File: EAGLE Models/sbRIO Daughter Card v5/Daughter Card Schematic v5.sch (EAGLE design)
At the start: 67 parts, among them IC1 BTS716G, IC2 BTS716G, IC3 BTS716G, Q7 MMBT4403-7-F, Q8 MMBT4403-7-F, U2 ADXL345, U3 L3G4200D

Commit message: made more changes to daughter card
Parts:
- removed F10, F9: (no value), resistor:R-EU_R0402
- added F11, F12: (no value), resistor:R-EU_R0402
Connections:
- removed net N$22: F9.1, TUB_CONN-12.KL
- removed net N$23: F10.1, TUB_CONN-5.KL
- new net N$7: F11.1, TUB_CONN-3.KL
- new net N$8: F12.1, TUB_CONN-1.KL
- net 12V: now also F11.2
- net 5V: now also F12.2; no longer F10.2, F9.2
- net AI3: now also TUB_CONN-11.KL; no longer TUB_CONN-10.KL
- net AI4: now also TUB_CONN-12.KL; no longer TUB_CONN-9.KL
- net AMS_OUT: now also TUB_CONN-6.KL; no longer TUB_CONN-3.KL
- net BSPD_OUT: now also TUB_CONN-4.KL; no longer TUB_CONN-1.KL
- net BUZZER_OUT: now also TUB_CONN-7.KL; no longer TUB_CONN-4.KL
- net CAN_H: now also TUB_CONN-9.KL; no longer TUB_CONN-7.KL
- net CAN_L: now also TUB_CONN-8.KL; no longer TUB_CONN-6.KL
- net DI02: now also TUB_CONN-2.KL; no longer TUB_CONN-8.KL
- net GND: now also TUB_CONN-10.KL; no longer TUB_CONN-11.KL
- net IMD_OUT: now also TUB_CONN-5.KL; no longer TUB_CONN-2.KL
- net STEERING_POS: now also TUB_CONN-16.KL; no longer TUB_CONN-14.KL
- net THROTTLE_1: now also TUB_CONN-15.KL; no longer TUB_CONN-16.KL
- net THROTTLE_2: now also TUB_CONN-14.KL; no longer TUB_CONN-15.KL
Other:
- moved on the sheet: R36, TUB_CONN-1, TUB_CONN-10, TUB_CONN-11, TUB_CONN-12, TUB_CONN-13, TUB_CONN-14, TUB_CONN-15, TUB_CONN-16, TUB_CONN-2, TUB_CONN-3, TUB_CONN-4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

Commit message: more daughter card  revisions
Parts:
- removed F11, F12: (no value), resistor:R-EU_R0402
- added F10, F9: (no value), resistor:R-EU_R0402
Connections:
- removed net DI02: TUB_CONN-2.KL
- removed net N$7: F11.1, TUB_CONN-3.KL
- removed net N$8: F12.1, TUB_CONN-1.KL
- new net DIO64: U$3.DIO64, U3.INT2
- new net DIO65: U$3.DIO65, U3.INT1
- new net N$16: F9.1, TUB_CONN-3.KL
- new net N$17: F10.1, TUB_CONN-1.KL
- net 12V: now also F9.2; no longer F11.2
- net 5V: now also F10.2; no longer F12.2
- net AI7: now also TUB_CONN-15.KL; no longer TUB_CONN-13.KL
- net DIO0: now also U2.SCL, U3.SCL
- net DIO2: now also TUB_CONN-2.KL
- net DIO32: now also U3.CS; no longer U2.SCL, U3.SCL
- net DIO33: no longer U3.CS
- net DIO34: no longer U3.INT1
- net DIO35: no longer U3.INT2
- net THROTTLE_1: now also TUB_CONN-13.KL; no longer TUB_CONN-15.KL
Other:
- moved on the sheet: TUB_CONN-1, TUB_CONN-10, TUB_CONN-11, TUB_CONN-12, TUB_CONN-13, TUB_CONN-14, TUB_CONN-15, TUB_CONN-16, TUB_CONN-2, TUB_CONN-3, TUB_CONN-4, TUB_CONN-5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

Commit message: FINISHED DAUGHTER CARD LAYOUT
haven't run DRC  yet
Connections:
- new net DIO40: IC1G$1.IN3, U$3.DIO40
- new net DIO41: IC1G$1.IN2, U$3.DIO41
- new net DIO42: IC3G$1.IN3, U$3.DIO42
- new net DIO43: IC3G$1.IN2, U$3.DIO43
- net AI10: now also AIO_PO_CONN-7.KL; no longer AIO_PO_CONN-5.KL
- net AI8: now also AIO_PO_CONN-5.KL; no longer AIO_PO_CONN-7.KL
- net AO0: now also F15.1; no longer F22.1
- net AO1: now also F20.1; no longer F21.1
- net AO2: now also F21.1; no longer F20.1
- net AO3: now also F22.1; no longer F15.1
- net DIO10: now also IC3G$1.IN4
- net DIO11: now also IC3G$1.IN1
- net DIO12: now also R36.2, TUB_CONN-2.KL
- net DIO2: no longer R36.2, TUB_CONN-2.KL
- net DIO21: no longer IC2G$1.IN2
- net DIO22: no longer IC2G$1.IN3
- net DIO25: no longer IC1G$1.IN1
- net DIO26: no longer IC1G$1.IN2
- net DIO27: no longer IC1G$1.IN3
- net DIO28: no longer IC1G$1.IN4
- net DIO38: now also IC2G$1.IN3
- net DIO39: now also IC2G$1.IN2
- net DIO6: now also IC2G$1.IN4; no longer IC2G$1.IN1
- net DIO7: now also IC2G$1.IN1; no longer IC2G$1.IN4
- net DIO8: now also IC1G$1.IN4
- net DIO9: now also IC1G$1.IN1
- net DIO90: no longer IC3G$1.IN3
- net DIO91: no longer IC3G$1.IN4
- net DIO92: no longer IC3G$1.IN1
- net DIO93: no longer IC3G$1.IN2
- net GND: now also IC2G$1.GND1/2, IC2G$1.GND3/4

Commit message: Routed extra DIO, because it was easy
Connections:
- new net DIO89: SBRIO_AUX.DIO18
- net DIO90: now also SBRIO_AUX.DIO19
- net DIO91: now also SBRIO_AUX.DIO38
- net DIO92: now also SBRIO_AUX.DIO15
- net DIO93: now also SBRIO_AUX.DIO14
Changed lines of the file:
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@@
 <wire x1="144.78" y1="20.32" x2="139.7" y2="20.32" width="0.1524" layer="91"/>
+</segment>
+<segment>
+<pinref part="SBRIO_AUX" gate="G$1" pin="DIO14"/>
+<wire x1="-66.04" y1="33.02" x2="-73.66" y2="33.02" width="0.1524" layer="91"/>
+<label x="-73.66" y="33.02" size="1.778" layer="95" rot="R180" xref="yes"/>
 </segment>
 </net>
@@
 <wire x1="144.78" y1="15.24" x2="142.24" y2="15.24" width="0.1524" layer="91"/>
 </segment>
+<segment>
+<pinref part="SBRIO_AUX" gate="G$1" pin="DIO15"/>
+<wire x1="-66.04" y1="30.48" x2="-73.66" y2="30.48" width="0.1524" layer="91"/>
+<label x="-73.66" y="30.48" size="1.778" layer="95" rot="R180" xref="yes"/>
+</segment>
 </net>
 <net name="DIO91" class="0">
@@
 <wire x1="144.78" y1="12.7" x2="142.24" y2="12.7" width="0.1524" layer="91"/>
 </segment>
+<segment>
+<pinref part="SBRIO_AUX" gate="G$1" pin="DIO38"/>
+<wire x1="-66.04" y1="17.78" x2="-73.66" y2="17.78" width="0.1524" layer="91"/>
+<label x="-73.66" y="17.78" size="1.778" layer="95" rot="R180" xref="yes"/>
+</segment>
 </net>
 <net name="DIO90" class="0">
@@
 <pinref part="U$3" gate="G$1" pin="DIO90"/>
 <wire x1="144.78" y1="7.62" x2="139.7" y2="7.62" width="0.1524" layer="91"/>
+</segment>
+<segment>
+<pinref part="SBRIO_AUX" gate="G$1" pin="DIO19"/>
+<wire x1="-66.04" y1="20.32" x2="-73.66" y2="20.32" width="0.1524" layer="91"/>
+<label x="-73.66" y="20.32" size="1.778" layer="95" rot="R180" xref="yes"/>
 </segment>
 </net>
@@
 </segment>
 </net>
+<net name="DIO89" class="0">
+<segment>
+<pinref part="SBRIO_AUX" gate="G$1" pin="DIO18"/>
+<wire x1="-66.04" y1="22.86" x2="-73.66" y2="22.86" width="0.1524" layer="91"/>
+<label x="-73.66" y="22.86" size="1.778" layer="95" rot="R180" xref="yes"/>
+</segment>
+</net>

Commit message: fixing drc errors
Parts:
- added X1: 5566-2, con-molex:5566-2
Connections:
- removed net N$5: U$3.VCC
- net 12V: now also X1-1.S, X1-2.S
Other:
- moved on the sheet: D3, D6, R9
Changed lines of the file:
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@@
 <part name="F9" library="resistor" deviceset="R-EU_" device="R0402"/>
 <part name="F10" library="resistor" deviceset="R-EU_" device="R0402"/>
+<part name="X1" library="con-molex" deviceset="5566-2" device=""/>
 </parts>
 <sheets>
@@
 <instance part="U$3" gate="G$1" x="200.66" y="7.62"/>
 <instance part="5V_REG" gate="G$1" x="35.56" y="91.44" rot="R270"/>
-<instance part="D3" gate="G$1" x="-38.1" y="7.62" rot="R90"/>
+<instance part="D3" gate="G$1" x="-27.94" y="17.78" rot="R90"/>
 <instance part="D1" gate="G$1" x="-91.44" y="50.8"/>
 <instance part="SHTDWN_CONN" gate="G$1" x="416.56" y="-71.12" rot="R180"/>
-<instance part="D6" gate="G$1" x="68.58" y="-53.34" rot="R270"/>
+<instance part="D6" gate="G$1" x="71.12" y="-38.1" rot="R270"/>
 <instance part="D5" gate="G$1" x="66.04" y="-43.18" rot="R270"/>
 <instance part="R36" gate="G$1" x="228.6" y="-88.9" rot="R270"/>
@@
 <instance part="D2" gate="G$1" x="-93.98" y="38.1"/>
 <instance part="R8" gate="G$1" x="71.12" y="-25.4" rot="R180"/>
-<instance part="R9" gate="G$1" x="73.66" y="-33.02"/>
+<instance part="R9" gate="G$1" x="76.2" y="-30.48" rot="R90"/>
 <instance part="F3" gate="G$1" x="403.86" y="-35.56" rot="MR0"/>
 <instance part="F4" gate="G$1" x="403.86" y="-40.64" rot="MR0"/>
@@
 <instance part="F9" gate="G$1" x="200.66" y="-193.04" rot="R90"/>
 <instance part="F10" gate="G$1" x="195.58" y="-182.88" rot="R90"/>
+<instance part="X1" gate="-1" x="299.72" y="-167.64" rot="R270"/>
+<instance part="X1" gate="-2" x="294.64" y="-167.64" rot="R270"/>
 </instances>
 <busses>
@@
 <junction x="195.58" y="86.36"/>
 <pinref part="5V_REG" gate="G$1" pin="GND"/>
-<wire x1="45.72" y1="88.9" x2="43.18" y2="88.9" width="0.1524" layer="91"/>
-<wire x1="2.54" y1="45.72" x2="2.54" y2="48.26" width="0.1524" layer="91"/>
 <label x="119.38" y="68.58" size="1.778" layer="95" xref="yes"/>
+<junction x="20.32" y="99.06"/>
+<junction x="129.54" y="86.36"/>
 </segment>
 <segment>
@@
 <wire x1="271.78" y1="104.14" x2="281.94" y2="104.14" width="0.1524" layer="91"/>
 <junction x="271.78" y="104.14"/>
+<junction x="261.62" y="104.14"/>
 </segment>
 <segment>
@@
 <pinref part="R9" gate="G$1" pin="2"/>
 <pinref part="R8" gate="G$1" pin="1"/>
-<wire x1="78.74" y1="-33.02" x2="78.74" y2="-25.4" width="0.1524" layer="91"/>
-<wire x1="78.74" y1="-25.4" x2="76.2" y2="-25.4" width="0.1524" layer="91"/>
-<wire x1="78.74" y1="-25.4" x2="86.36" y2="-25.4" width="0.1524" layer="91"/>
-<junction x="78.74" y="-25.4"/>
+<wire x1="76.2" y1="-25.4" x2="86.36" y2="-25.4" width="0.1524" layer="91"/>
+<junction x="76.2" y="-25.4"/>
 <label x="86.36" y="-25.4" size="1.778" layer="95"/>
 </segment>
@@
 <segment>
 <pinref part="D3" gate="G$1" pin="C"/>
-<wire x1="-38.1" y1="10.16" x2="-38.1" y2="104.14" width="0.1524" layer="91"/>
-<wire x1="-38.1" y1="104.14" x2="58.42" y2="104.14" width="0.1524" layer="91"/>
+<wire x1="-27.94" y1="20.32" x2="-27.94" y2="104.14" width="0.1524" layer="91"/>
+<wire x1="-27.94" y1="104.14" x2="58.42" y2="104.14" width="0.1524" layer="91"/>
 <wire x1="58.42" y1="104.14" x2="58.42" y2="93.98" width="0.1524" layer="91"/>
 <pinref part="3.3V_REG" gate="G$1" pin="IN"/>
@@
 <wire x1="45.72" y1="93.98" x2="58.42" y2="93.98" width="0.1524" layer="91"/>
 <junction x="58.42" y="93.98"/>
+<junction x="99.06" y="93.98"/>
 </segment>
 <segment>
@@
 <wire x1="264.16" y1="-165.1" x2="264.16" y2="-170.18" width="0.1524" layer="91"/>
 <label x="264.16" y="-170.18" size="1.778" layer="95" rot="R270" xref="yes"/>
-<wire x1="264.16" y1="-165.1" x2="261.62" y2="-167.64" width="0.1524" layer="91"/>
 <wire x1="264.16" y1="-165.1" x2="269.24" y2="-165.1" width="0.1524" layer="91"/>
 <wire x1="269.24" y1="-165.1" x2="271.78" y2="-165.1" width="0.1524" layer="91"/>
@@
 <wire x1="281.94" y1="-165.1" x2="284.48" y2="-165.1" width="0.1524" layer="91"/>
 <wire x1="284.48" y1="-165.1" x2="287.02" y2="-165.1" width="0.1524" layer="91"/>
-<wire x1="287.02" y1="-165.1" x2="302.26" y2="-165.1" width="0.1524" layer="91"/>
+<wire x1="287.02" y1="-165.1" x2="294.64" y2="-165.1" width="0.1524" layer="91"/>
+<wire x1="294.64" y1="-165.1" x2="299.72" y2="-165.1" width="0.1524" layer="91"/>
+<wire x1="299.72" y1="-165.1" x2="302.26" y2="-165.1" width="0.1524" layer="91"/>
 <wire x1="302.26" y1="-165.1" x2="304.8" y2="-162.56" width="0.1524" layer="91"/>
-<junction x="264.16" y="-165.1"/>
 <wire x1="304.8" y1="-162.56" x2="304.8" y2="-157.48" width="0.1524" layer="91"/>
 <pinref part="IC1" gate="G$2" pin="VBB@1"/>
@@
 <junction x="304.8" y="-142.24"/>
 <pinref part="IC3" gate="G$2" pin="VBB@8"/>
+<junction x="304.8" y="-139.7"/>
+<pinref part="X1" gate="-1" pin="S"/>
+<junction x="299.72" y="-165.1"/>
+<pinref part="X1" gate="-2" pin="S"/>
+<junction x="294.64" y="-165.1"/>
 </segment>
 <segment>
@@
 <wire x1="345.44" y1="-73.66" x2="347.98" y2="-73.66" width="0.1524" layer="91"/>
 <label x="347.98" y="-73.66" size="1.778" layer="95" xref="yes"/>
-<wire x1="345.44" y1="-73.66" x2="345.44" y2="-55.88" width="0.1524" layer="91"/>
+<wire x1="345.44" y1="-73.66" x2="345.44" y2="-71.12" width="0.1524" layer="91"/>
+<junction x="345.44" y="-55.88"/>
+<junction x="345.44" y="-58.42"/>
+<wire x1="345.44" y1="-71.12" x2="345.44" y2="-68.58" width="0.1524" layer="91"/>
+<wire x1="345.44" y1="-68.58" x2="345.44" y2="-66.04" width="0.1524" layer="91"/>
+<wire x1="345.44" y1="-66.04" x2="345.44" y2="-63.5" width="0.1524" layer="91"/>
+<wire x1="345.44" y1="-63.5" x2="345.44" y2="-60.96" width="0.1524" layer="91"/>
+<wire x1="345.44" y1="-60.96" x2="345.44" y2="-58.42" width="0.1524" layer="91"/>
+<wire x1="345.44" y1="-58.42" x2="345.44" y2="-55.88" width="0.1524" layer="91"/>
+<junction x="345.44" y="-60.96"/>
+<junction x="345.44" y="-63.5"/>
+<junction x="345.44" y="-66.04"/>
+<junction x="345.44" y="-68.58"/>
+<junction x="345.44" y="-71.12"/>
+<junction x="345.44" y="-73.66"/>
 </segment>
 <segment>
@@
 <pinref part="D3" gate="G$1" pin="A"/>
 <pinref part="SBRIO_ANALOG" gate="G$1" pin="AI0"/>
-<wire x1="-38.1" y1="5.08" x2="-27.94" y2="5.08" width="0.1524" layer="91"/>
+<wire x1="-27.94" y1="15.24" x2="-27.94" y2="5.08" width="0.1524" layer="91"/>
 <wire x1="-27.94" y1="5.08" x2="2.54" y2="5.08" width="0.1524" layer="91"/>
-<wire x1="-38.1" y1="5.08" x2="-38.1" y2="7.62" width="0.1524" layer="91"/>
 <pinref part="R13" gate="G$1" pin="2"/>
 <wire x1="-27.94" y1="2.54" x2="-27.94" y2="5.08" width="0.1524" layer="91"/>
@@
 <pinref part="5V_REG" gate="G$1" pin="5V"/>
 <wire x1="27.94" y1="91.44" x2="30.48" y2="91.44" width="0.1524" layer="91"/>
+<junction x="20.32" y="91.44"/>
+<junction x="27.94" y="91.44"/>
 </segment>
 <segment>
@@
 <segment>
 <pinref part="D6" gate="G$1" pin="C"/>
-<wire x1="68.58" y1="-149.86" x2="68.58" y2="-55.88" width="0.1524" layer="91"/>
+<wire x1="68.58" y1="-149.86" x2="71.12" y2="-40.64" width="0.1524" layer="91"/>
 <label x="71.12" y="-129.54" size="1.778" layer="95" rot="R270"/>
 <pinref part="F8" gate="G$1" pin="2"/>
@@
 <pinref part="ACCUMULATOR_CONN" gate="G$1" pin="S@1"/>
 <wire x1="60.96" y1="-185.42" x2="60.96" y2="-182.88" width="0.1524" layer="91"/>
+<junction x="60.96" y="-182.88"/>
+<junction x="60.96" y="-185.42"/>
+<junction x="60.96" y="-187.96"/>
+<junction x="60.96" y="-190.5"/>
+<junction x="83.82" y="-180.34"/>
 </segment>
 </net>
@@
 <wire x1="33.02" y1="-111.76" x2="33.02" y2="-78.74" width="0.1524" layer="91"/>
 <wire x1="33.02" y1="-78.74" x2="22.86" y2="-78.74" width="0.1524" layer="91"/>
-<wire x1="22.86" y1="-78.74" x2="22.86" y2="-38.1" width="0.1524" layer="91"/>
-<wire x1="22.86" y1="-38.1" x2="40.64" y2="-38.1" width="0.1524" layer="91"/>
+<wire x1="22.86" y1="-78.74" x2="22.86" y2="-40.64" width="0.1524" layer="91"/>
+<wire x1="22.86" y1="-40.64" x2="40.64" y2="-40.64" width="0.1524" layer="91"/>
 <pinref part="U$2" gate="G$1" pin="SHIELD"/>
-<wire x1="40.64" y1="-38.1" x2="40.64" y2="-48.26" width="0.1524" layer="91"/>
+<wire x1="40.64" y1="-40.64" x2="40.64" y2="-48.26" width="0.1524" layer="91"/>
 <label x="33.02" y="-111.76" size="1.778" layer="95" rot="R270"/>
 </segment>
@@
 <pinref part="C8" gate="G$1" pin="1"/>
 <junction x="162.56" y="114.3"/>
+<junction x="129.54" y="93.98"/>
+<junction x="119.38" y="93.98"/>
 </segment>
 <segment>
@@
 <junction x="271.78" y="111.76"/>
 <junction x="281.94" y="111.76"/>
+<junction x="261.62" y="111.76"/>
 </segment>
 </net>
@@
 <wire x1="325.12" y1="96.52" x2="335.28" y2="96.52" width="0.1524" layer="91"/>
 <wire x1="335.28" y1="96.52" x2="335.28" y2="81.28" width="0.1524" layer="91"/>
+<junction x="325.12" y="96.52"/>
 </segment>
 </net>
@@
 </segment>
 </net>
-<net name="N$5" class="0">
-<segment>
-<pinref part="U$3" gate="G$1" pin="VCC"/>
-<wire x1="172.72" y1="-30.48" x2="175.26" y2="-30.48" width="0.1524" layer="91"/>
-</segment>
-</net>
 <net name="DIO95" class="0">
 <segment>
@@
 <segment>
 <pinref part="D6" gate="G$1" pin="A"/>
-<wire x1="68.58" y1="-50.8" x2="68.58" y2="-33.02" width="0.1524" layer="91"/>
-<wire x1="68.58" y1="-33.02" x2="68.58" y2="38.1" width="0.1524" layer="91"/>
+<wire x1="71.12" y1="-35.56" x2="76.2" y2="-35.56" width="0.1524" layer="91"/>
+<wire x1="76.2" y1="-35.56" x2="83.82" y2="-35.56" width="0.1524" layer="91"/>
 <pinref part="R9" gate="G$1" pin="1"/>
-<junction x="68.58" y="-33.02"/>
-<label x="68.58" y="38.1" size="1.778" layer="95" xref="yes"/>
-</segment>
-</net>
+<junction x="76.2" y="-35.56"/>
+<label x="83.82" y="-35.56" size="1.778" layer="95" xref="yes"/>
+<junction x="71.12" y="-35.56"/>
+</segment>
+</net>

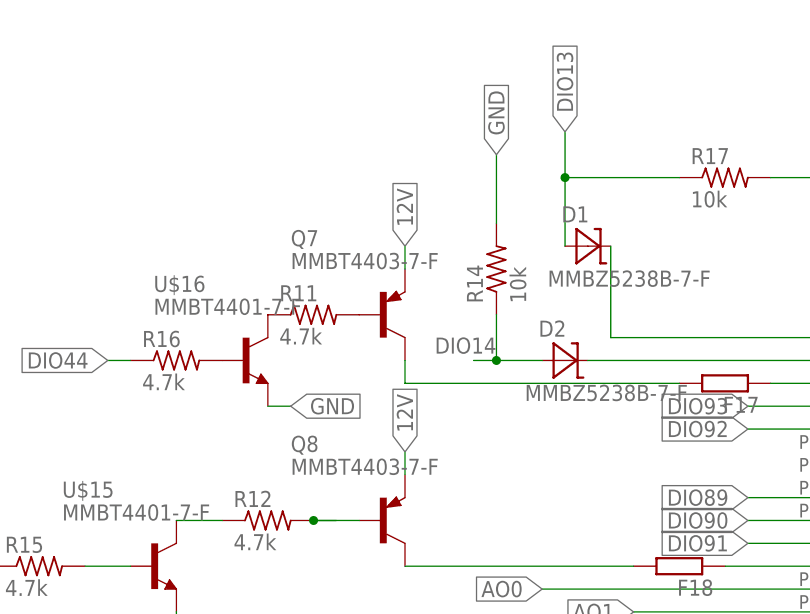
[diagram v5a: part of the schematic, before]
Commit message: Added pours and molex connector for amplified 12V
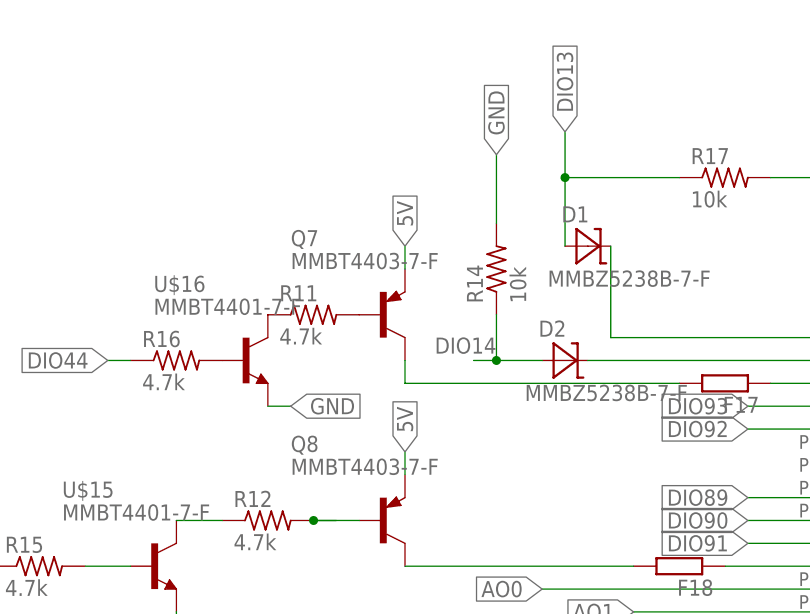
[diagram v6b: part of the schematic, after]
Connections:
- net 12V: no longer Q7.E, Q8.E
- net 5V: now also Q7.E, Q8.E
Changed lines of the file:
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@@
-</segment>
-<segment>
-<pinref part="Q7" gate="G$1" pin="E"/>
-<wire x1="-111.76" y1="48.26" x2="-111.76" y2="50.8" width="0.1524" layer="91"/>
-<label x="-111.76" y="50.8" size="1.778" layer="95" rot="R90" xref="yes"/>
-</segment>
-<segment>
-<pinref part="Q8" gate="G$1" pin="E"/>
-<wire x1="-111.76" y1="25.4" x2="-111.76" y2="27.94" width="0.1524" layer="91"/>
-<label x="-111.76" y="27.94" size="1.778" layer="95" rot="R90" xref="yes"/>
 </segment>
 <segment>
@@
 <label x="195.58" y="-149.86" size="1.778" layer="95" rot="R90" xref="yes"/>
 </segment>
+<segment>
+<pinref part="Q7" gate="G$1" pin="E"/>
+<wire x1="-111.76" y1="48.26" x2="-111.76" y2="50.8" width="0.1524" layer="91"/>
+<label x="-111.76" y="50.8" size="1.778" layer="95" rot="R90" xref="yes"/>
+</segment>
+<segment>
+<pinref part="Q8" gate="G$1" pin="E"/>
+<wire x1="-111.76" y1="25.4" x2="-111.76" y2="27.94" width="0.1524" layer="91"/>
+<label x="-111.76" y="27.94" size="1.778" layer="95" rot="R90" xref="yes"/>
+</segment>
 </net>
